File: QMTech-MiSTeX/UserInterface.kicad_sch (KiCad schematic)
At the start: 81 parts, among them CN1 PJ-325C5-BL, CN2 U.FL-R-SMT-1(80), CN3 U.FL-R-SMT-1(80), CN4 U.FL-R-SMT-1(80), CN5 U.FL-R-SMT-1(80), J15 Conn_01x02_Pin, J16 Conn_01x02_Pin, J17 Conn_01x02_Pin, J8 Conn_01x02_Pin, SW1 TS-1187A-B-A-B, SW2 TS-1187A-B-A-B, SW3 TS-1187A-B-A-B, SW4 TS-1187A-B-A-B, SW5 XKB5858-W-F-75, SW6 XKB5858-W-F-75, SW7 DSHP04TSGER, U5 ZGY133/T10(PLT)

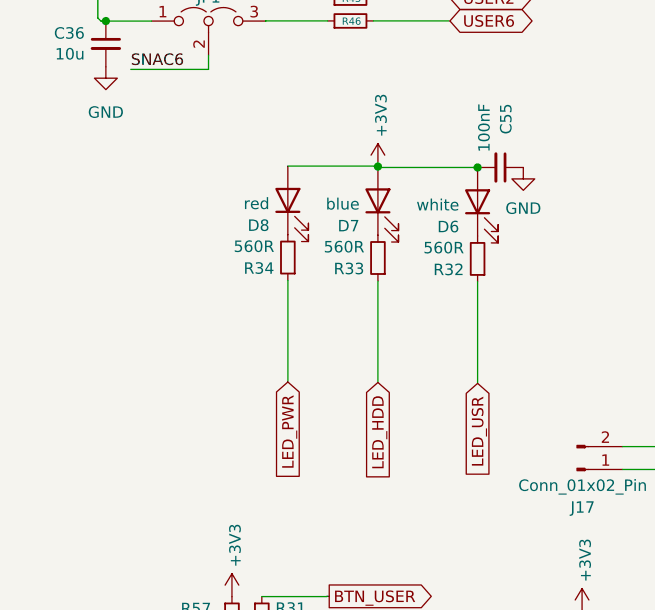
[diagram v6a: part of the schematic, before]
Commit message: add headers for LEDs
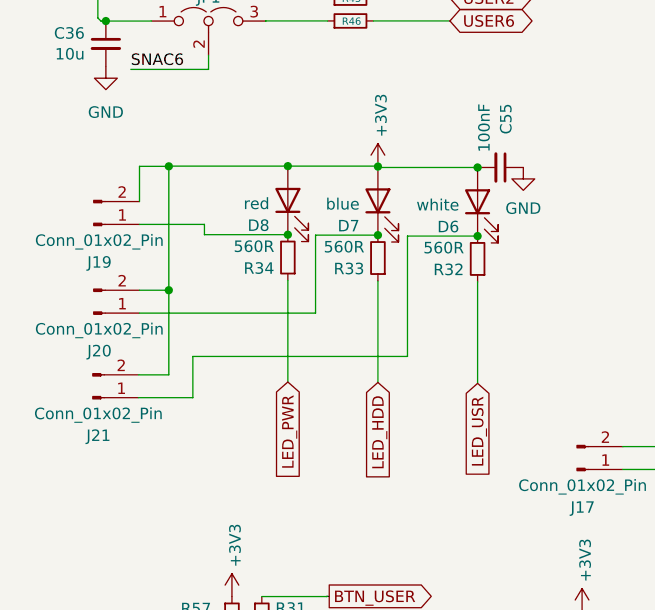
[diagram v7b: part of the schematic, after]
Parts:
- added J19, J20, J21: Conn_01x02_Pin, Connector_PinHeader_2.54mm:PinHeader_1x02_P2.54mm_Vertical, symbol Connector:Conn_01x02_Pin
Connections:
- net +3V3: now also J19.2 (Pin_2), J20.2 (Pin_2), J21.2 (Pin_2)
- net at D8.1 (K), R34.2: now also J19.1 (Pin_1)
- net at D7.1 (K), R33.2: now also J20.1 (Pin_1)
- net at D6.1 (K), R32.2: now also J21.1 (Pin_1)
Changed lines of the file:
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@@
   (junction (at 44.8818 68.58) (diameter 0) (color 0 0 0 0)
   )
+  (junction (at 42.9514 124.079) (diameter 0) (color 0 0 0 0)
+  )
   (junction (at 74.295 65.405) (diameter 0) (color 0 0 0 0)
   )
@@
   (junction (at 34.9504 179.9336) (diameter 0) (color 0 0 0 0)
   )
+  (junction (at 29.7238 130.2512) (diameter 0) (color 0 0 0 0)
+  )
+  (junction (at 52.959 124.1298) (diameter 0) (color 0 0 0 0)
+  )
   (junction (at 118.11 93.98) (diameter 0) (color 0 0 0 0)
   )
@@
   (junction (at 203.2 161.29) (diameter 0) (color 0 0 0 0)
   )
+  (junction (at 42.9514 116.459) (diameter 0) (color 0 0 0 0)
+  )
   (junction (at 40.0599 169.3672) (diameter 0) (color 0 0 0 0)
   )
   (junction (at 75.6412 171.0182) (diameter 0) (color 0 0 0 0)
   )
+  (junction (at 29.7238 116.4844) (diameter 0) (color 0 0 0 0)
+  )
   (junction (at 190.5 143.51) (diameter 0) (color 0 0 0 0)
   )
@@
   (junction (at 73.8514 181.5846) (diameter 0) (color 0 0 0 0)
   )
+  (junction (at 64.0334 124.2314) (diameter 0) (color 0 0 0 0)
+  )
   (junction (at 31.3182 18.9484) (diameter 0) (color 0 0 0 0)
   )
@@
     (stroke (width 0) (type default))
   )
+  (wire (pts (xy 46.0299 132.7912) (xy 26.4668 132.7912))
+    (stroke (width 0) (type default))
+  )
   (wire (pts (xy 175.26 161.29) (xy 175.26 156.21))
     (stroke (width 0.254) (type default))
@@
     (stroke (width 0) (type default))
   )
+  (wire (pts (xy 32.3932 142.1892) (xy 26.3652 142.1892))
+    (stroke (width 0) (type default))
+  )
   (wire (pts (xy 40.0599 169.3672) (xy 45.5471 169.3672))
     (stroke (width 0) (type default))
@@
     (stroke (width 0) (type default))
   )
+  (wire (pts (xy 33.6804 122.936) (xy 26.4668 122.936))
+    (stroke (width 0) (type default))
+  )
   (wire (pts (xy 36.195 19.05) (xy 36.1442 19.05))
     (stroke (width 0) (type default))
@@
     (stroke (width 0) (type default))
   )
+  (wire (pts (xy 29.7238 116.4844) (xy 26.4668 116.4844))
+    (stroke (width 0) (type default))
+  )
   (wire (pts (xy 60.96 100.33) (xy 52.4453 100.33))
     (stroke (width 0) (type default))
@@
     (stroke (width 0) (type default))
   )
+  (wire (pts (xy 56.2429 124.2314) (xy 56.2429 137.6072))
+    (stroke (width 0) (type default))
+  )
   (wire (pts (xy 53.3641 68.58) (xy 44.8818 68.58))
     (stroke (width 0) (type default))
@@
     (stroke (width 0.254) (type default))
   )
+  (wire (pts (xy 42.9514 124.079) (xy 33.6804 124.079))
+    (stroke (width 0) (type default))
+  )
   (wire (pts (xy 36.7402 169.3672) (xy 40.0599 169.3672))
     (stroke (width 0) (type default))
@@
     (stroke (width 0) (type default))
   )
+  (wire (pts (xy 42.9514 116.459) (xy 29.7238 116.459))
+    (stroke (width 0) (type default))
+  )
   (wire (pts (xy 21.8383 97.7113) (xy 21.8383 99.9973))
     (stroke (width 0) (type default))
@@
     (stroke (width 0) (type default))
   )
+  (wire (pts (xy 29.7238 130.2512) (xy 29.7238 139.6492))
+    (stroke (width 0) (type default))
+  )
   (wire (pts (xy 47.3653 100.33) (xy 40.499 100.33))
     (stroke (width 0) (type default))
@@
     (stroke (width 0) (type default))
   )
+  (wire (pts (xy 46.0299 124.1298) (xy 46.0299 132.7912))
+    (stroke (width 0) (type default))
+  )
   (wire (pts (xy 65.571 179.0446) (xy 71.5654 179.0446))
     (stroke (width 0) (type default))
@@
     (stroke (width 0) (type default))
   )
+  (wire (pts (xy 52.959 124.1298) (xy 46.0299 124.1298))
+    (stroke (width 0) (type default))
+  )
   (wire (pts (xy 210.82 143.51) (xy 215.9 143.51))
     (stroke (width 0) (type default))
@@
     (stroke (width 0) (type default))
   )
+  (wire (pts (xy 29.7238 139.6492) (xy 26.3652 139.6492))
+    (stroke (width 0) (type default))
+  )
   (wire (pts (xy 71.1167 31.75) (xy 71.1167 31.8007))
     (stroke (width 0) (type default))
@@
     (stroke (width 0) (type default))
   )
+  (wire (pts (xy 29.7238 116.4844) (xy 29.7238 130.2512))
+    (stroke (width 0) (type default))
+  )
   (wire (pts (xy 139.7 133.2499) (xy 147.32 133.2499))
     (stroke (width 0) (type default))
@@
     (stroke (width 0) (type default))
   )
+  (wire (pts (xy 29.7238 116.459) (xy 29.7238 116.4844))
+    (stroke (width 0) (type default))
+  )
   (wire (pts (xy 32.6644 175.26) (xy 32.6644 170.8452))
     (stroke (width 0) (type default))
@@
     (stroke (width 0) (type default))
   )
+  (wire (pts (xy 33.6804 124.079) (xy 33.6804 122.936))
+    (stroke (width 0) (type default))
+  )
   (wire (pts (xy 187.96 151.13) (xy 190.5 151.13))
     (stroke (width 0.254) (type default))
@@
     (stroke (width 0) (type default))
   )
+  (wire (pts (xy 56.2429 137.6072) (xy 32.3932 137.6072))
+    (stroke (width 0) (type default))
+  )
   (wire (pts (xy 34.9504 177.8) (xy 34.9504 179.9336))
     (stroke (width 0) (type default))
@@
     (stroke (width 0) (type default))
   )
+  (wire (pts (xy 32.3932 137.6072) (xy 32.3932 142.1892))
+    (stroke (width 0) (type default))
+  )
   (wire (pts (xy 16.0541 66.04) (xy 24.5618 66.04))
     (stroke (width 0) (type default))
@@
     (stroke (width 0) (type default))
   )
+  (wire (pts (xy 64.0334 124.2314) (xy 56.2429 124.2314))
+    (stroke (width 0) (type default))
+  )
   (wire (pts (xy 105.672 180.467) (xy 111.6664 180.467))
     (stroke (width 0) (type default))
@@
     (stroke (width 0) (type default))
   )
+  (wire (pts (xy 26.4668 116.4844) (xy 26.4668 120.396))
+    (stroke (width 0) (type default))
+  )
   (wire (pts (xy 84.4481 171.0182) (xy 84.4481 173.9646))
     (stroke (width 0) (type default))
@@
     (stroke (width 0.254) (type default))
   )
+  (wire (pts (xy 29.7238 130.2512) (xy 26.4668 130.2512))
+    (stroke (width 0) (type default))
+  )
   (wire (pts (xy 66.3272 24.13) (xy 61.595 24.13))
     (stroke (width 0) (type default))
@@
     )
   )
+  (symbol (lib_id "Connector:Conn_01x02_Pin") (at 21.3868 132.7912 0) (mirror x) (unit 1)
+    (in_bom yes) (on_board yes) (dnp no)
+    (property "Reference" "J20" (at 22.0218 137.0117 0)
+      (effects (font (size 1.27 1.27)))
+    )
+    (property "Value" "Conn_01x02_Pin" (at 22.0218 134.5875 0)
+      (effects (font (size 1.27 1.27)))
+    )
+    (property "Footprint" "Connector_PinHeader_2.54mm:PinHeader_1x02_P2.54mm_Vertical" (at 21.3868 132.7912 0)
+      (effects (font (size 1.27 1.27)) hide)
+    )
+    (property "Datasheet" "~" (at 21.3868 132.7912 0)
+      (effects (font (size 1.27 1.27)) hide)
+    )
+    (pin "2")
+    (pin "1")
+    (instances
+      (project "QMTech-MiSTeX"
+        (path "/bf95850e-2fcb-4784-a603-f17fc357556b/cce2b405-ae09-44af-ba42-d113d6ffe521"
+          (reference "J20") (unit 1)
+        )
+      )
+    )
+  )
   (symbol (lib_id "jlcpcb-basic-resistor:R_0402_4.7k") (at 115.7478 169.9006 0) (unit 1)
     (in_bom yes) (on_board yes) (dnp no)
@@
     )
   )
+  (symbol (lib_id "Connector:Conn_01x02_Pin") (at 21.3868 122.936 0) (mirror x) (unit 1)
+    (in_bom yes) (on_board yes) (dnp no)
+    (property "Reference" "J19" (at 22.0218 127.1565 0)
+      (effects (font (size 1.27 1.27)))
+    )
+    (property "Value" "Conn_01x02_Pin" (at 22.0218 124.7323 0)
+      (effects (font (size 1.27 1.27)))
+    )
+    (property "Footprint" "Connector_PinHeader_2.54mm:PinHeader_1x02_P2.54mm_Vertical" (at 21.3868 122.936 0)
+      (effects (font (size 1.27 1.27)) hide)
+    )
+    (property "Datasheet" "~" (at 21.3868 122.936 0)
+      (effects (font (size 1.27 1.27)) hide)
+    )
+    (pin "2")
+    (pin "1")
+    (instances
+      (project "QMTech-MiSTeX"
+        (path "/bf95850e-2fcb-4784-a603-f17fc357556b/cce2b405-ae09-44af-ba42-d113d6ffe521"
+          (reference "J19") (unit 1)
+        )
+      )
+    )
+  )
   (symbol (lib_id "Connector:Conn_01x02_Pin") (at 21.59 177.8 0) (mirror x) (unit 1)
     (in_bom yes) (on_board yes) (dnp no)
@@
         )
       )
+    )
+  )
+  (symbol (lib_id "Connector:Conn_01x02_Pin") (at 21.2852 142.1892 0) (mirror x) (unit 1)
+    (in_bom yes) (on_board yes) (dnp no)
+    (property "Reference" "J21" (at 21.9202 146.4097 0)
+      (effects (font (size 1.27 1.27)))
+    )
+    (property "Value" "Conn_01x02_Pin" (at 21.9202 143.9855 0)
+      (effects (font (size 1.27 1.27)))
+    )
+    (property "Footprint" "Connector_PinHeader_2.54mm:PinHeader_1x02_P2.54mm_Vertical" (at 21.2852 142.1892 0)
+      (effects (font (size 1.27 1.27)) hide)
+    )
+    (property "Datasheet" "~" (at 21.2852 142.1892 0)
+      (effects (font (size 1.27 1.27)) hide)
+    )
+    (pin "2")
+    (pin "1")
+    (instances
+      (project "QMTech-MiSTeX"
+        (path "/bf95850e-2fcb-4784-a603-f17fc357556b/cce2b405-ae09-44af-ba42-d113d6ffe521"
+          (reference "J21") (unit 1)
+        )
+      )

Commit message: fix side switches, vias under uFL connectors, silk screen
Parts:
- SW5, SW6: LCSC Part C780037 -> C780036
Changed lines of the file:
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@@
       (effects (font (size 1.27 1.27)) hide)
     )
-    (property "LCSC Part" "C780037" (at 170.18 133.2499 0)
+    (property "LCSC Part" "C780036" (at 170.18 133.2499 0)
       (effects (font (size 1.27 1.27)) hide)
     )
@@
       (effects (font (size 1.27 1.27)) hide)
     )
-    (property "LCSC Part" "C780037" (at 149.86 147.32 0)
-      (effects (font (size 1.27 1.27)) hide)
-    )
+    (property "LCSC Part" "C780036" (at 149.86 147.32 0)
+      (effects (font (size 1.27 1.27)) hide)
+    )
